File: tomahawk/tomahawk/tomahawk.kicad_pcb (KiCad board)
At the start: 2 copper layers, 79 parts, among them SW1 SW_Push, SW10 SW_Push, SW11 SW_Push, SW12 SW_Push, SW13 SW_Push, SW14 SW_Push, SW15 SW_Push, SW16 SW_Push, SW17 SW_Push, SW18 SW_Push, SW19 SW_Push, SW2 SW_Push, SW20 SW_Push, SW21 SW_Push, SW22 SW_Push, SW23 SW_Push, SW24 SW_Push, SW25 SW_Push, SW26 SW_Push, SW27 SW_Push, SW28 SW_Push, SW29 SW_Push, SW3 SW_Push, SW30 SW_Push, SW31 SW_Push, SW32 SW_Push, SW33 SW_Push, SW34 SW_Push, SW35 SW_Push, SW36 SW_Push, SW37 SW_Push, SW38 SW_Push, SW39 SW_Push, SW4 SW_Push, SW5 SW_Push, SW6 SW_Push, SW7 SW_Push, SW8 SW_Push, SW9 SW_Push

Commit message: updated footprints and pcb
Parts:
- SW1, SW10, SW11, SW12, SW13, SW14, SW15, SW16, SW17, SW18, SW19, SW2, SW20, SW21, SW22, SW23, SW24, SW25, SW26, SW27, SW28, SW29, SW3, SW30, SW31, SW32, SW33, SW34, SW35, SW36, SW37, SW38, SW39, SW4, SW5, SW6, SW7, SW8, SW9: footprint Keyswitches:Kailh_socket_PG1350 -> Foostan:keyswitch_choc12_hotswap_1u
- U1: footprint ProMicro_RP2040:pro_micro_rp2040 -> ProMicro RP2040:pro_micro_rp2040

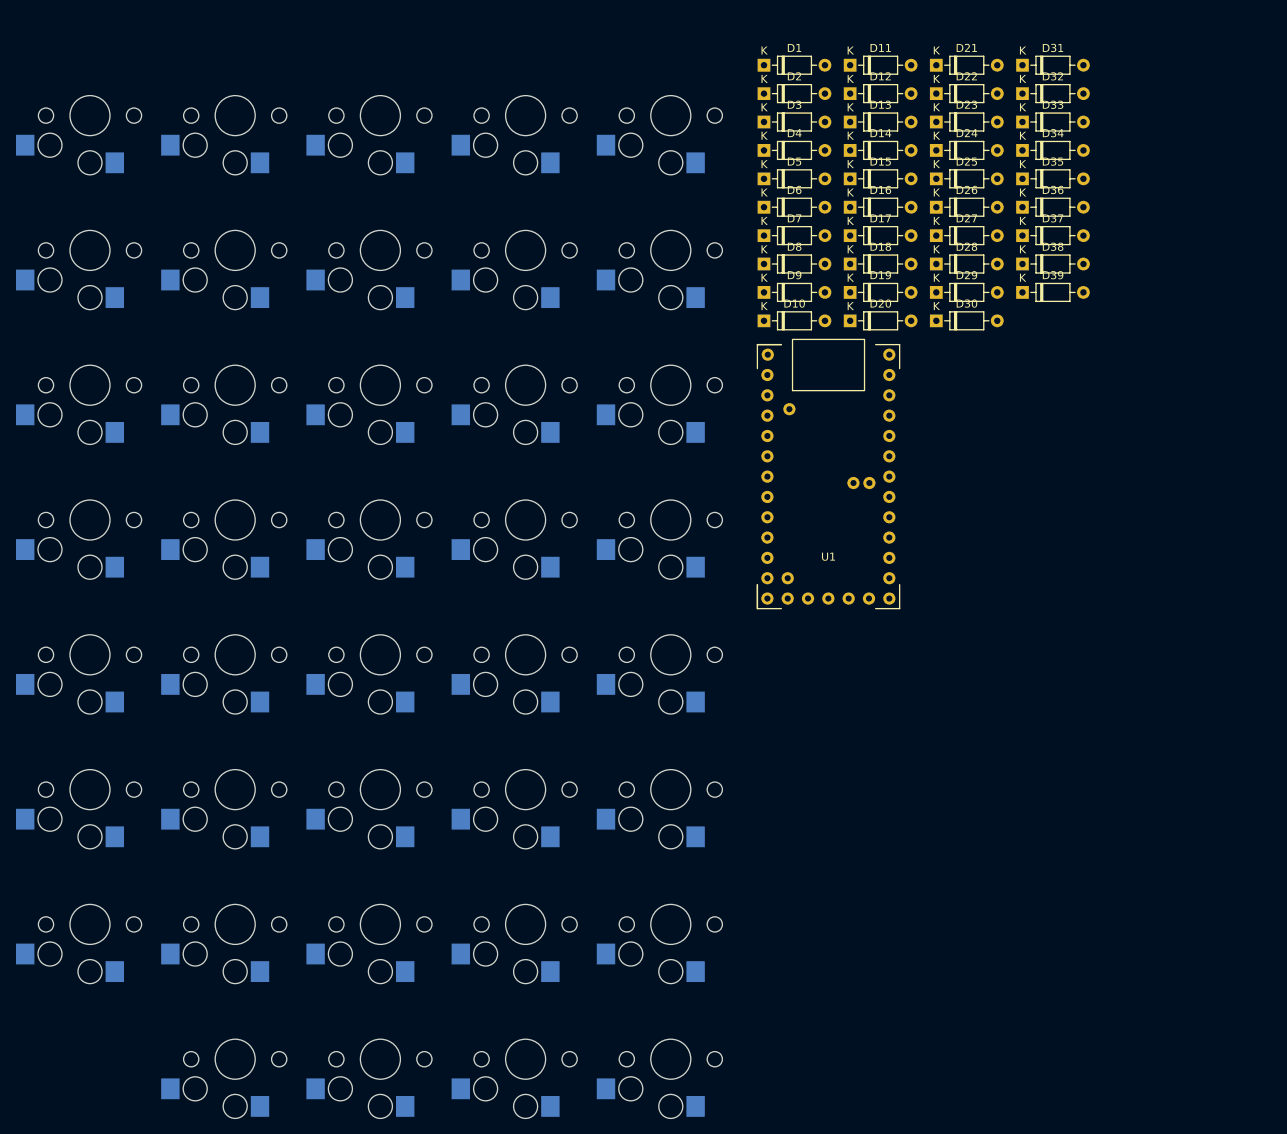
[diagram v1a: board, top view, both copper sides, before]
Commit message: updated layout and pcb
- still need to work on the thumb cluster
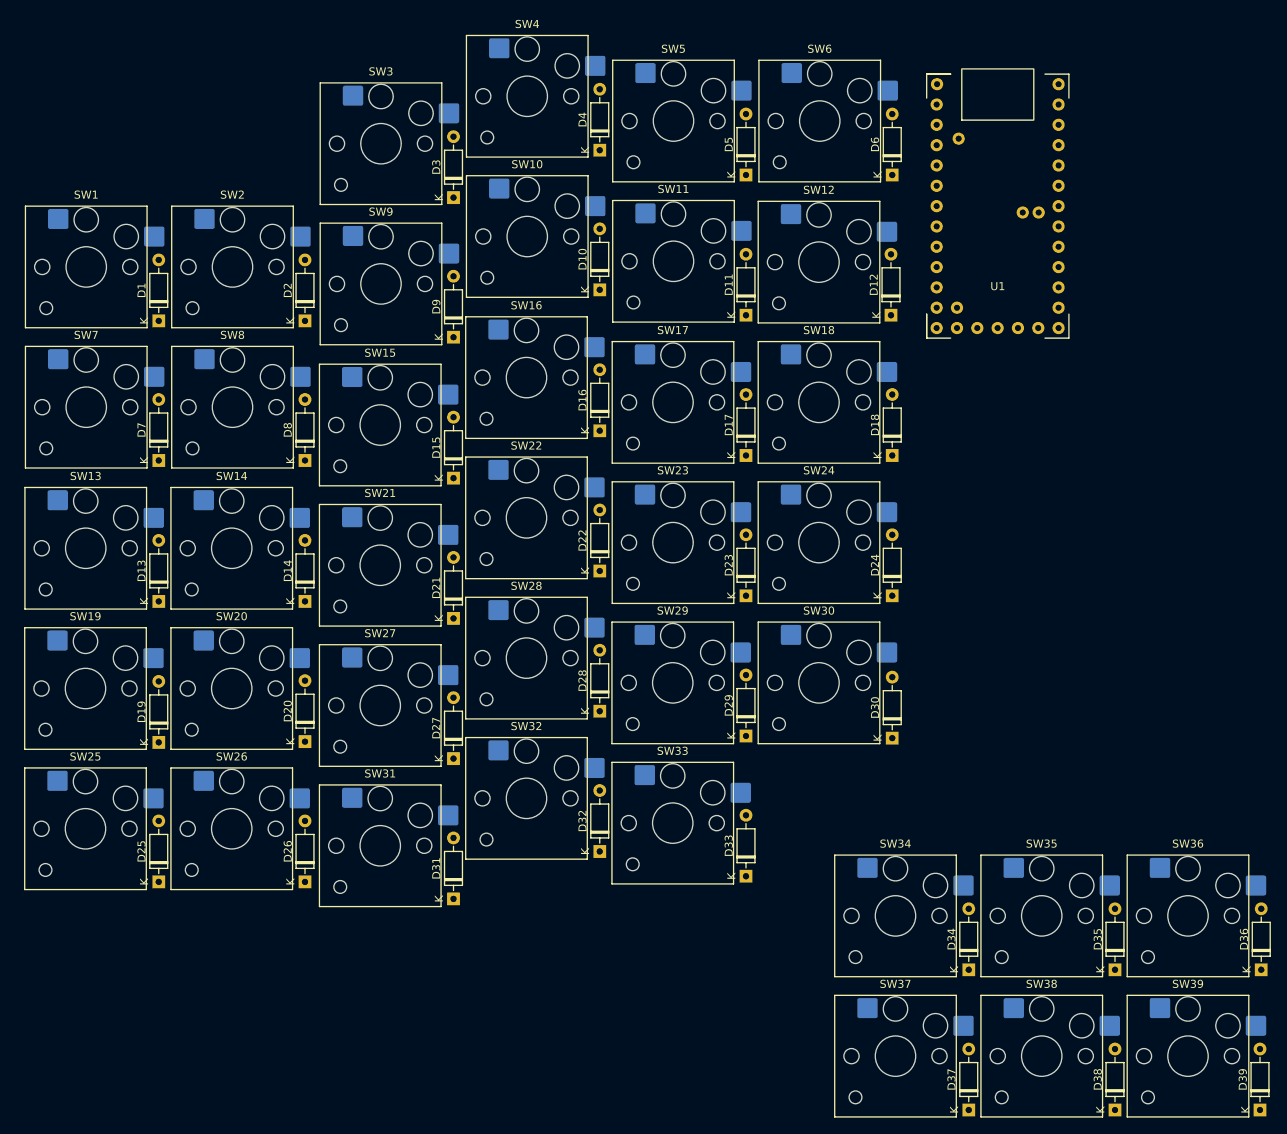
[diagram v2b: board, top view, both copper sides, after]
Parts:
- SW1, SW10, SW11, SW12, SW13, SW14, SW15, SW16, SW17, SW18, SW19, SW2, SW20, SW21, SW22, SW23, SW24, SW25, SW26, SW27, SW28, SW29, SW3, SW30, SW31, SW32, SW33, SW34, SW35, SW36, SW37, SW38, SW39, SW4, SW5, SW6, SW7, SW8, SW9: footprint Foostan:keyswitch_choc12_hotswap_1u -> Scotto Hotswap:Hotswap_Choc_V1V2_1.00u; moved to F.Cu
- moved SW36 145.9 mm to (194.8, 135.7), turned to 0 degrees
- moved SW39 138.2 mm to (194.8, 153.3), turned to 0 degrees
- moved SW35 136.2 mm to (176.5, 135.7), turned to 0 degrees
- moved D25 131.0 mm to (66.1, 131.5), turned to 90 degrees
- moved SW34 130.6 mm to (158.2, 135.7), turned to 0 degrees
- moved D31 126.2 mm to (102.9, 133.6), turned to 90 degrees
- moved SW38 123.5 mm to (176.5, 153.3), turned to 0 degrees
- moved D26 115.5 mm to (84.4, 131.5), turned to 90 degrees
- moved SW33 114.6 mm to (130.3, 124.1), turned to 0 degrees
- moved SW37 112.5 mm to (158.2, 153.3), turned to 0 degrees
- moved D37 109.5 mm to (167.3, 160.0), turned to 90 degrees
- moved D32 108.5 mm to (121.2, 127.7), turned to 90 degrees
- moved D39 106.4 mm to (203.8, 160.0), turned to 90 degrees
- moved D38 106.4 mm to (185.6, 160.0), turned to 90 degrees
- moved D13 105.2 mm to (66.1, 96.4), turned to 90 degrees
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
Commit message: rough tracks
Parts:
- moved U1 3.22 mm to (164.1, 61.0)
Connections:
- U1 pad 14: TROW1 -> TROW2
- U1 pad 15: TROW2 -> TROW1
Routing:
- net COL5: track 0.00 -> 401.9 mm
- net COL4: track 0.00 -> 336.7 mm
- net COL3: track 0.00 -> 285.4 mm
- net COL2: track 0.00 -> 199.8 mm
- net COL1: track 0.00 -> 199.7 mm
- net ROW5: track 0.00 -> 164.3 mm
- net ROW4: track 0.00 -> 143.8 mm
- net TROW2: track 0.00 -> 139.9 mm
- net COL6: track 0.00 -> 135.8 mm
- net ROW3: track 0.00 -> 128.1 mm
- net ROW6: track 0.00 -> 126.0 mm
- net TROW1: track 0.00 -> 122.7 mm
- net ROW1: track 0.00 -> 116.1 mm
- net ROW2: track 0.00 -> 114.0 mm
- net Net-(D30-A): track 0.00 -> 3.36 mm
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
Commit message: WIP: need to fix thumb cluster
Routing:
- net COL1: track 199.7 -> 70.3 mm
- net TROW2: track 139.9 -> 38.0 mm
- net TROW1: track 122.7 -> 36.6 mm
- net COL4: track 336.7 -> 264.7 mm
- net COL3: track 285.4 -> 213.7 mm
- net COL5: track 401.9 -> 334.6 mm
- net ROW6: track 126.0 -> 138.9 mm
- net COL6: track 135.8 -> 142.2 mm
- net COL2: track 199.8 -> 203.3 mm
- net ROW5: track 164.3 -> 166.3 mm
- net ROW4: track 143.8 -> 144.8 mm

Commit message: wip
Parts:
- moved D25 238.1 mm to (286.4, 41.3), turned to 0 degrees
- moved D31 221.5 mm to (297.2, 27.1), turned to 0 degrees
- moved D26 219.8 mm to (286.4, 44.9), turned to 0 degrees
- moved D13 218.6 mm to (275.7, 34.2), turned to 0 degrees
- moved D19 217.6 mm to (275.7, 55.5), turned to 0 degrees
- moved D1 201.7 mm to (264.9, 27.1), turned to 0 degrees
- moved D7 201.1 mm to (264.9, 48.4), turned to 0 degrees
- moved D32 200.9 mm to (297.2, 30.7), turned to 0 degrees
- moved D14 200.1 mm to (275.7, 37.8), turned to 0 degrees
- moved D20 199.0 mm to (275.7, 59.1), turned to 0 degrees
- moved D21 196.9 mm to (286.4, 27.1), turned to 0 degrees
- moved D27 195.6 mm to (286.4, 48.4), turned to 0 degrees
- moved D33 184.9 mm to (297.2, 34.2), turned to 0 degrees
- moved D2 183.1 mm to (264.9, 30.7), turned to 0 degrees
- moved D8 182.5 mm to (264.9, 52.0), turned to 0 degrees
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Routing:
- net COL5: track 334.6 -> 0.00 mm
- net COL4: track 264.7 -> 0.00 mm
- net COL3: track 213.7 -> 0.00 mm
- net COL2: track 203.3 -> 0.00 mm
- net ROW5: track 166.3 -> 0.00 mm
- net ROW4: track 144.8 -> 0.00 mm
- net COL6: track 142.2 -> 0.00 mm
- net ROW6: track 138.9 -> 0.00 mm
- net ROW3: track 128.1 -> 0.00 mm
- net ROW1: track 116.1 -> 0.00 mm
- net ROW2: track 114.0 -> 0.00 mm
- net COL1: track 70.3 -> 0.00 mm
- net TROW2: track 38.0 -> 0.00 mm
- net TROW1: track 36.6 -> 0.00 mm
- net Net-(D30-A): track 3.36 -> 0.00 mm
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
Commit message: WIP: aligned layout, updated design and net class rules
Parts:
- moved D25 248.4 mm to (56.0, 134.2), turned to 90 degrees
- moved D31 232.6 mm to (92.0, 136.6), turned to 90 degrees
- moved D26 230.4 mm to (74.0, 134.2), turned to 90 degrees
- moved D13 229.3 mm to (56.0, 100.2), turned to 90 degrees
- moved D19 228.1 mm to (56.0, 117.2), turned to 90 degrees
- moved D1 212.5 mm to (56.0, 66.2), turned to 90 degrees
- moved D7 211.8 mm to (56.0, 83.2), turned to 90 degrees
- moved D32 211.3 mm to (110.0, 128.6), turned to 90 degrees
- moved D14 211.1 mm to (74.0, 100.2), turned to 90 degrees
- moved D20 209.9 mm to (74.0, 117.2), turned to 90 degrees
- moved D21 208.5 mm to (92.0, 102.6), turned to 90 degrees
- moved D27 207.0 mm to (92.0, 119.6), turned to 90 degrees
- moved D33 195.7 mm to (128.0, 132.6), turned to 90 degrees
- moved D2 194.2 mm to (74.0, 66.2), turned to 90 degrees
- moved D8 193.4 mm to (74.0, 83.2), turned to 90 degrees
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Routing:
- net ROW5: track 0.00 -> 109.4 mm
- net ROW4: track 0.00 -> 109.4 mm
- net ROW3: track 0.00 -> 109.4 mm
- net ROW1: track 0.00 -> 109.3 mm
- net ROW2: track 0.00 -> 109.3 mm
- net COL5: track 0.00 -> 85.0 mm
- net COL4: track 0.00 -> 85.0 mm
- net COL3: track 0.00 -> 85.0 mm
- net COL6: track 0.00 -> 68.0 mm
- net COL2: track 0.00 -> 68.0 mm
- net COL1: track 0.00 -> 68.0 mm
- net ROW6: track 0.00 -> 44.4 mm

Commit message: wip updated diode positioning, and placed thumb cluster
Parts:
- D1, D10, D11, D12, D13, D14, D15, D16, D17, D18, D19, D2, D20, D21, D22, D23, D24, D25, D26, D27, D28, D29, D3, D30, D31, D32, D33, D34, D35, D36, D37, D38, D39, D4, D5, D6, D7, D8, D9: moved to B.Cu
- moved D39 98.8 mm to (169.4, 185.8), turned to 30 degrees
- moved D38 88.4 mm to (159.1, 169.3), turned to 45 degrees
- moved SW39 87.2 mm to (170.7, 174.7), turned to -60 degrees
- moved D37 85.3 mm to (145.0, 155.9), turned to 60 degrees
- moved SW36 80.9 mm to (184.7, 160.7), turned to -60 degrees
- moved D36 76.7 mm to (183.3, 171.8), turned to 30 degrees
- moved SW38 72.4 mm to (157.4, 158.2), turned to -45 degrees
- moved SW35 64.3 mm to (171.5, 144.2), turned to -45 degrees
- moved SW37 64.3 mm to (140.5, 145.6), turned to -30 degrees
- moved D35 63.5 mm to (173.1, 155.3), turned to 45 degrees
- moved D34 58.2 mm to (158.9, 142.0), turned to 60 degrees
- moved SW34 53.9 mm to (154.5, 131.7), turned to -30 degrees
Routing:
- net COL5: track 85.0 -> 175.6 mm
- net COL4: track 85.0 -> 167.2 mm
- net COL3: track 85.0 -> 153.6 mm
- net TROW1: track 0.00 -> 40.5 mm
- net TROW2: track 0.00 -> 40.4 mm
- net Net-(D34-A): track 0.00 -> 3.16 mm
- net Net-(D37-A): track 0.00 -> 3.16 mm
- net Net-(D31-A): track 0.00 -> 3.09 mm
- net Net-(D9-A): track 0.00 -> 3.09 mm
- net Net-(D8-A): track 0.00 -> 3.09 mm
- net Net-(D7-A): track 0.00 -> 3.09 mm
- net Net-(D6-A): track 0.00 -> 3.09 mm
- net Net-(D5-A): track 0.00 -> 3.09 mm
- net Net-(D4-A): track 0.00 -> 3.09 mm
- net Net-(D33-A): track 0.00 -> 3.09 mm
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
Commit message: wip
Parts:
- removed U1: ~, ProMicro RP2040:pro_micro_rp2040
- added U2: nice_nano, Scotto MCU:Nice_Nano_V2, F.Cu at (168.5, 51.9)
- D1, D10, D11, D12, D13, D14, D15, D16, D17, D18, D19, D2, D20, D21, D22, D23, D24, D25, D26, D27, D28, D29, D3, D30, D31, D32, D33, D34, D35, D36, D37, D38, D39, D4, D5, D6, D7, D8, D9: footprint Diode_THT:D_DO-35_SOD27_P7.62mm_Horizontal -> Diode_SMD:D_SOD-123
- moved D30 2.61 mm to (145.8, 114.8)
- moved D19 2.61 mm to (55.8, 114.6)
- moved D38 1.60 mm to (160.2, 168.3), turned to 47 degrees
- moved D35 1.59 mm to (174.3, 154.2), turned to 47 degrees
- moved D34 1.31 mm to (159.5, 140.8)
- moved D10 1.31 mm to (109.9, 59.3)
- moved D16 1.31 mm to (109.9, 76.3)
- moved D4 1.31 mm to (109.9, 42.3)
- moved D21 1.31 mm to (91.9, 101.3)
- moved D27 1.31 mm to (91.9, 118.3)
- moved D9 1.31 mm to (91.9, 67.3)
- moved D22 1.30 mm to (109.9, 93.3)
- moved D28 1.30 mm to (109.9, 110.3)
- moved D32 1.30 mm to (109.9, 127.3)
- moved D11 1.30 mm to (127.9, 63.3)
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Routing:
- net COL5: track 175.6 -> 0.00 mm
- net COL4: track 167.2 -> 0.00 mm
- net COL3: track 153.6 -> 0.00 mm
- net ROW5: track 109.4 -> 0.00 mm
- net ROW4: track 109.4 -> 0.00 mm
- net ROW3: track 109.4 -> 0.00 mm
- net ROW1: track 109.3 -> 0.00 mm
- net ROW2: track 109.3 -> 0.00 mm
- net COL6: track 68.0 -> 0.00 mm
- net COL2: track 68.0 -> 0.00 mm
- net COL1: track 68.0 -> 0.00 mm
- net ROW6: track 44.4 -> 0.00 mm
- net TROW1: track 40.5 -> 0.00 mm
- net TROW2: track 40.4 -> 0.00 mm
- net Net-(D34-A): track 3.16 -> 0.00 mm
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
